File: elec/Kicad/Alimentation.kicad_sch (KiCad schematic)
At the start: 37 parts, among them J7 USB_B_Micro_MAIN, Q1 SI2323DS-T1, Q5 NTK3043NT1G, SW4 SW_ON/OFF, U9 TLV62085RLTR

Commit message: commencer le PCB vite fait
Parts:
- removed SW4: SW_ON/OFF, SINGLE_DIP_SWITCH:SW_DS04-254-2-01BK-SMT, symbol Switch:SW_SPST
- removed TP1: 3.3V, TestPoint:TestPoint_Loop_D1.80mm_Drill1.0mm_Beaded, symbol Connector:TestPoint
- removed TP3: 5V, TestPoint:TestPoint_Loop_D1.80mm_Drill1.0mm_Beaded, symbol Connector:TestPoint
- removed TP9: BAT_PERCENT, TestPoint:TestPoint_Loop_D1.80mm_Drill1.0mm_Beaded, symbol Connector:TestPoint
- added S1: SW_ON/OFF, SINGLE_DIP_SWITCH:SW_DS04-254-2-01BK-SMT, symbol DS04-254-2-01BK-SMT:DS04-254-2-01BK-SMT
- U9: footprint RLT0007A -> TLV62085RLTR:RLT0007A
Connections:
- net Vbat: now also S1.1B
- net at D7.1 (K), Q1.3 (D): now also S1.1A

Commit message: touillerie
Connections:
- net GND: now also C34.2, R31.2
- net Vbat: no longer C25.1, R4.1, R6.1, S1.1B, U9.1 (EN), U9.7 (VIN)
- net at R30.2, U9.2 (PG): no longer C34.2, R31.2
- new net Vin: C25.1, R4.1, R6.1, S1.1B, U9.1 (EN), U9.7 (VIN)
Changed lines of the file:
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@@
 	(paper "A4")
 	(junction
-		(at 27.94 57.15)
+		(at 88.9 92.71)
+		(diameter 0)
+		(color 0 0 0 0)
+	)
+	(junction
+		(at 125.73 92.71)
 		(diameter 0)
 		(color 0 0 0 0)
@@
 	)
 	(junction
+		(at 39.37 57.15)
+		(diameter 0)
+		(color 0 0 0 0)
+	)
+	(junction
 		(at 226.06 33.02)
 		(diameter 0)
@@
 	)
 	(junction
-		(at 125.73 87.63)
-		(diameter 0)
-		(color 0 0 0 0)
-	)
-	(junction
 		(at 88.9 146.05)
 		(diameter 0)
@@
 	)
 	(junction
-		(at 115.57 87.63)
-		(diameter 0)
-		(color 0 0 0 0)
-	)
-	(junction
 		(at 125.73 52.07)
 		(diameter 0)
@@
 	(wire
 		(pts
-			(xy 142.24 87.63) (xy 125.73 87.63)
+			(xy 142.24 92.71) (xy 125.73 92.71)
 		)
 		(stroke
@@
 	(wire
 		(pts
-			(xy 142.24 71.12) (xy 142.24 87.63)
+			(xy 142.24 71.12) (xy 142.24 92.71)
 		)
 		(stroke
@@
 	(wire
 		(pts
-			(xy 125.73 87.63) (xy 115.57 87.63)
-		)
-		(stroke
-			(width 0)
-			(type default)
-		)
-	)
-	(wire
-		(pts
-			(xy 27.94 57.15) (xy 44.45 57.15)
+			(xy 24.13 57.15) (xy 39.37 57.15)
 		)
 		(stroke
@@
 	(wire
 		(pts
+			(xy 88.9 92.71) (xy 125.73 92.71)
+		)
+		(stroke
+			(width 0)
+			(type default)
+		)
+	)
+	(wire
+		(pts
 			(xy 171.45 43.18) (xy 176.53 43.18)
 		)
@@
 	(wire
 		(pts
-			(xy 24.13 57.15) (xy 27.94 57.15)
-		)
-		(stroke
-			(width 0)
-			(type default)
-		)
-	)
-	(wire
-		(pts
 			(xy 77.47 146.05) (xy 88.9 146.05)
 		)
@@
 	(wire
 		(pts
-			(xy 27.94 52.07) (xy 27.94 57.15)
-		)
-		(stroke
-			(width 0)
-			(type default)
-		)
-	)
-	(wire
-		(pts
 			(xy 71.12 92.71) (xy 88.9 92.71)
 		)
@@
 	(wire
 		(pts
-			(xy 125.73 72.39) (xy 125.73 87.63)
+			(xy 125.73 72.39) (xy 125.73 92.71)
 		)
 		(stroke
@@
 		)
 	)
+	(wire
+		(pts
+			(xy 39.37 57.15) (xy 44.45 57.15)
+		)
+		(stroke
+			(width 0)
+			(type default)
+		)
+	)
 	(rectangle
 		(start 198.12 74.93)
@@
 		)
 	)
-	(global_label "Vbat"
-		(shape input)
-		(at 27.94 52.07 90)
-		(fields_autoplaced yes)
-		(effects
-			(font
-				(size 1.016 1.016)
-			)
-			(justify left)
-		)
-		(property "Intersheetrefs" "${INTERSHEET_REFS}"
-			(at 27.94 46.3922 90)
-			(effects
-				(font
-					(size 1.27 1.27)
-				)
-				(justify left)
-				(hide yes)
-			)
-		)
-	)
 	(global_label "BAT_PERCENT"
 		(shape output)
@@
 			)
 		)
-		(property "Datasheet" ""
+		(property "Datasheet" "https://www.digikey.ca/en/products/detail/onsemi/NTK3043NT1G/1484893"
 			(at 222.25 93.98 0)
 			(effects
@@
 					(unit 1)
 				)
+			)
+		)
+	)
+	(symbol
+		(lib_id "power:PWR_FLAG")
+		(at 39.37 57.15 0)
+		(unit 1)
+		(exclude_from_sim no)
+		(in_bom yes)
+		(on_board yes)
+		(dnp no)
+		(fields_autoplaced yes)
+		(property "Reference" "#FLG01"
+			(at 39.37 55.245 0)
+			(effects
+				(font
+					(size 1.27 1.27)
+				)
+				(hide yes)
+			)
+		)
+		(property "Value" "PWR_FLAG"
+			(at 39.37 52.07 0)
+			(effects
+				(font
+					(size 1.27 1.27)
+				)
+			)
+		)
+		(property "Footprint" ""
+			(at 39.37 57.15 0)
+			(effects
+				(font
+					(size 1.27 1.27)
+				)
+				(hide yes)
+			)
+		)
+		(property "Datasheet" "~"
+			(at 39.37 57.15 0)
+			(effects
+				(font
+					(size 1.27 1.27)
+				)
+				(hide yes)
+			)
+		)
+		(property "Description" "Special symbol for telling ERC where power comes from"
+			(at 39.37 57.15 0)
+			(effects
+				(font
+					(size 1.27 1.27)
+				)
+				(hide yes)
+			)
+		)
+		(pin "1"
+		)
+		(instances
+			(project "rulerSchematic"
+				(path "/a1545928-1195-40b9-b3c4-78f837012afb/47f0fc71-ff78-496f-bb04-036a9aeaa71c/6f59428e-8e72-4854-8d86-784df1ffb46d"
+					(reference "#FLG01")
+					(unit 1)
+				)

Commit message: Jpense pas boire jeudi sérieux vue que y'a pas de 5@8
routage du découplage et des CLK
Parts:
- C25, C26, C27, C28, C29, C30, C31, C32, C33, C34, C35: footprint Capacitor_SMD:C_0603_1608Metric_Pad1.08x0.95mm_HandSolder -> Capacitor_SMD:C_0402_1005Metric_Pad0.74x0.62mm_HandSolder
- R10, R11, R2, R28, R29, R30, R31, R4, R5, R6: footprint Resistor_SMD:R_0603_1608Metric_Pad0.98x0.95mm_HandSolder -> Resistor_SMD:R_0402_1005Metric_Pad0.72x0.64mm_HandSolder
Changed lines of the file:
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@@
 			)
 		)
-		(property "Footprint" "Resistor_SMD:R_0603_1608Metric_Pad0.98x0.95mm_HandSolder"
+		(property "Footprint" "Resistor_SMD:R_0402_1005Metric_Pad0.72x0.64mm_HandSolder"
 			(at 249.682 101.6 90)
 			(effects
@@
 			)
 		)
-		(property "Footprint" "Resistor_SMD:R_0603_1608Metric_Pad0.98x0.95mm_HandSolder"
+		(property "Footprint" "Resistor_SMD:R_0402_1005Metric_Pad0.72x0.64mm_HandSolder"
 			(at 234.95 94.742 90)
 			(effects
@@
 			)
 		)
-		(property "Footprint" "Capacitor_SMD:C_0603_1608Metric_Pad1.08x0.95mm_HandSolder"
+		(property "Footprint" "Capacitor_SMD:C_0402_1005Metric_Pad0.74x0.62mm_HandSolder"
 			(at 126.6952 72.39 0)
 			(effects
@@
 			)
 		)
-		(property "Footprint" "Resistor_SMD:R_0603_1608Metric_Pad0.98x0.95mm_HandSolder"
+		(property "Footprint" "Resistor_SMD:R_0402_1005Metric_Pad0.72x0.64mm_HandSolder"
 			(at 102.362 63.5 90)
 			(effects
@@
 			)
 		)
-		(property "Footprint" "Capacitor_SMD:C_0603_1608Metric_Pad1.08x0.95mm_HandSolder"
+		(property "Footprint" "Capacitor_SMD:C_0402_1005Metric_Pad0.74x0.62mm_HandSolder"
 			(at 92.4052 171.45 0)
 			(effects
@@
 			)
 		)
-		(property "Footprint" "Capacitor_SMD:C_0603_1608Metric_Pad1.08x0.95mm_HandSolder"
+		(property "Footprint" "Capacitor_SMD:C_0402_1005Metric_Pad0.74x0.62mm_HandSolder"
 			(at 113.9952 144.78 0)
 			(effects
@@
 			)
 		)
-		(property "Footprint" "Capacitor_SMD:C_0603_1608Metric_Pad1.08x0.95mm_HandSolder"
+		(property "Footprint" "Capacitor_SMD:C_0402_1005Metric_Pad0.74x0.62mm_HandSolder"
 			(at 65.7352 144.78 0)
 			(effects
@@
 			)
 		)
-		(property "Footprint" "Resistor_SMD:R_0603_1608Metric_Pad0.98x0.95mm_HandSolder"
+		(property "Footprint" "Resistor_SMD:R_0402_1005Metric_Pad0.72x0.64mm_HandSolder"
 			(at 221.488 109.22 90)
 			(effects
@@
 			)
 		)
-		(property "Footprint" "Capacitor_SMD:C_0603_1608Metric_Pad1.08x0.95mm_HandSolder"
+		(property "Footprint" "Capacitor_SMD:C_0402_1005Metric_Pad0.74x0.62mm_HandSolder"
 			(at 78.4352 144.78 0)
 			(effects
@@
 			)
 		)
-		(property "Footprint" "Resistor_SMD:R_0603_1608Metric_Pad0.98x0.95mm_HandSolder"
+		(property "Footprint" "Resistor_SMD:R_0402_1005Metric_Pad0.72x0.64mm_HandSolder"
 			(at 221.488 82.55 90)
 			(effects
@@
 			)
 		)
-		(property "Footprint" "Capacitor_SMD:C_0603_1608Metric_Pad1.08x0.95mm_HandSolder"
+		(property "Footprint" "Capacitor_SMD:C_0402_1005Metric_Pad0.74x0.62mm_HandSolder"
 			(at 196.5452 45.72 0)
 			(effects
@@
 			)
 		)
-		(property "Footprint" "Capacitor_SMD:C_0603_1608Metric_Pad1.08x0.95mm_HandSolder"
+		(property "Footprint" "Capacitor_SMD:C_0402_1005Metric_Pad0.74x0.62mm_HandSolder"
 			(at 103.8352 171.45 0)
 			(effects
@@
 			)
 		)
-		(property "Footprint" "Resistor_SMD:R_0603_1608Metric_Pad0.98x0.95mm_HandSolder"
+		(property "Footprint" "Resistor_SMD:R_0402_1005Metric_Pad0.72x0.64mm_HandSolder"
 			(at 113.792 68.58 90)
 			(effects
@@
 			)
 		)
-		(property "Footprint" "Resistor_SMD:R_0603_1608Metric_Pad0.98x0.95mm_HandSolder"
+		(property "Footprint" "Resistor_SMD:R_0402_1005Metric_Pad0.72x0.64mm_HandSolder"
 			(at 208.788 41.91 90)
 			(effects
@@
 			)
 		)
-		(property "Footprint" "Capacitor_SMD:C_0603_1608Metric_Pad1.08x0.95mm_HandSolder"
+		(property "Footprint" "Capacitor_SMD:C_0402_1005Metric_Pad0.74x0.62mm_HandSolder"
 			(at 101.2952 144.78 0)
 			(effects
@@
 			)
 		)
-		(property "Footprint" "Resistor_SMD:R_0603_1608Metric_Pad0.98x0.95mm_HandSolder"
+		(property "Footprint" "Resistor_SMD:R_0402_1005Metric_Pad0.72x0.64mm_HandSolder"
 			(at 227.838 43.18 90)
 			(effects
@@
 			)
 		)
-		(property "Footprint" "Resistor_SMD:R_0603_1608Metric_Pad0.98x0.95mm_HandSolder"
+		(property "Footprint" "Resistor_SMD:R_0402_1005Metric_Pad0.72x0.64mm_HandSolder"
 			(at 140.462 67.31 90)
 			(effects
@@
 			)
 		)
-		(property "Footprint" "Resistor_SMD:R_0603_1608Metric_Pad0.98x0.95mm_HandSolder"
+		(property "Footprint" "Resistor_SMD:R_0402_1005Metric_Pad0.72x0.64mm_HandSolder"
 			(at 102.362 78.74 90)
 			(effects
@@
 			)
 		)
-		(property "Footprint" "Capacitor_SMD:C_0603_1608Metric_Pad1.08x0.95mm_HandSolder"
+		(property "Footprint" "Capacitor_SMD:C_0402_1005Metric_Pad0.74x0.62mm_HandSolder"
 			(at 45.4152 71.12 0)
 			(effects
@@
 			)
 		)
-		(property "Footprint" "Capacitor_SMD:C_0603_1608Metric_Pad1.08x0.95mm_HandSolder"
+		(property "Footprint" "Capacitor_SMD:C_0402_1005Metric_Pad0.74x0.62mm_HandSolder"
 			(at 125.4252 144.78 0)
 			(effects
@@
 			)
 		)
-		(property "Footprint" "Capacitor_SMD:C_0603_1608Metric_Pad1.08x0.95mm_HandSolder"
+		(property "Footprint" "Capacitor_SMD:C_0402_1005Metric_Pad0.74x0.62mm_HandSolder"
 			(at 89.8652 144.78 0)
 			(effects

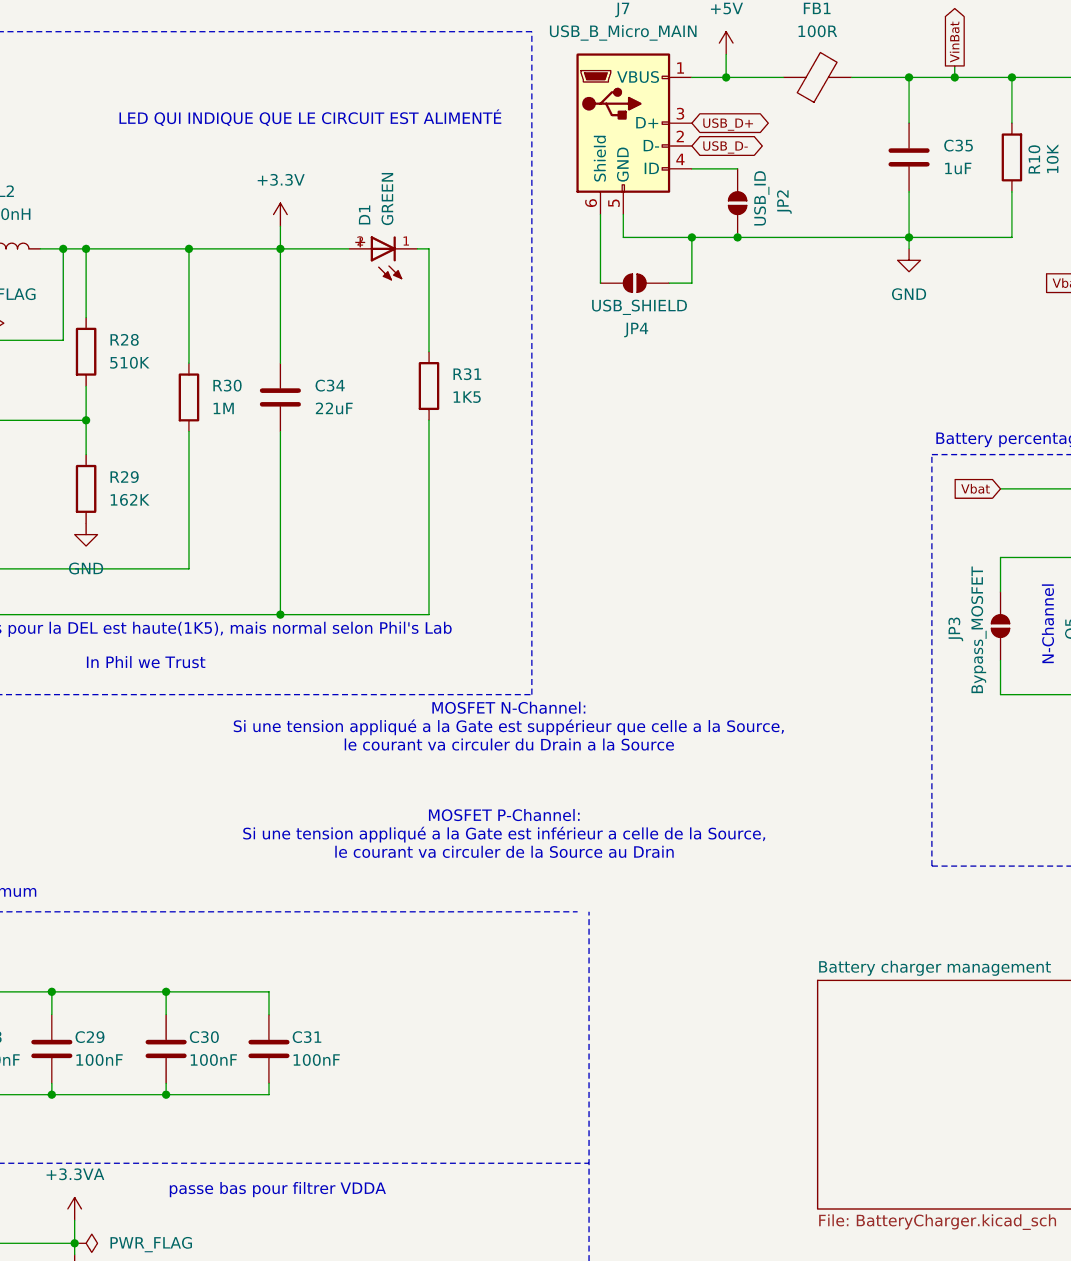
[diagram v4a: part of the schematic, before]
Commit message: modification du magnéto
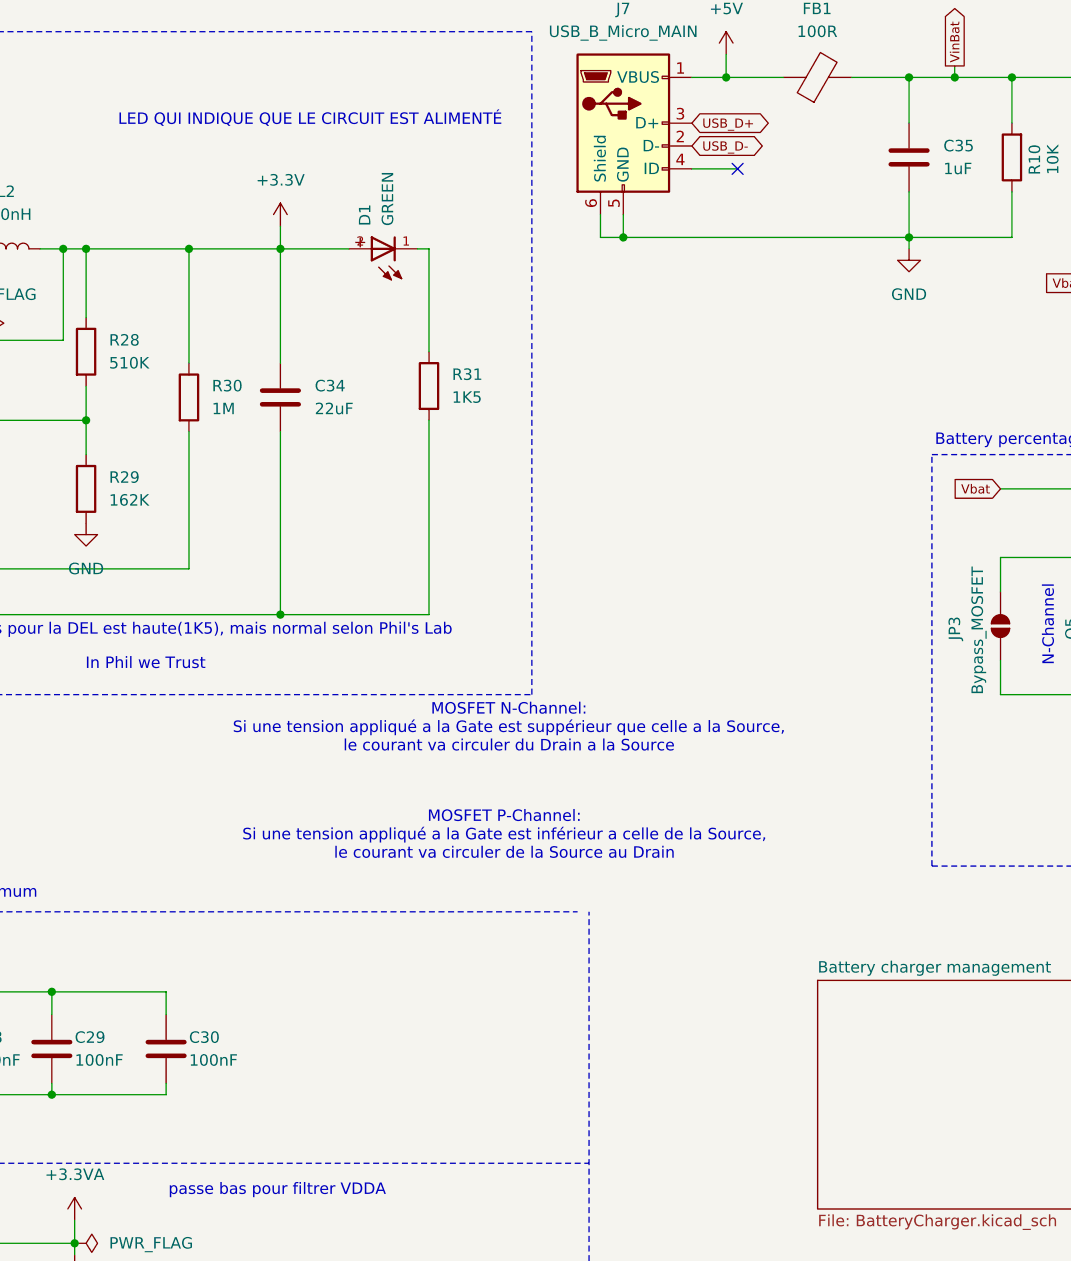
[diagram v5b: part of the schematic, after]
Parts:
- removed C31: 100nF, Capacitor_SMD:C_0402_1005Metric_Pad0.74x0.62mm_HandSolder, symbol Device:C
- removed JP2: USB_ID, Jumper:SolderJumper-2_P1.3mm_Open_TrianglePad1.0x1.5mm, symbol Jumper:SolderJumper_2_Open
- removed JP4: USB_SHIELD, Jumper:SolderJumper-2_P1.3mm_Open_TrianglePad1.0x1.5mm, symbol Jumper:SolderJumper_2_Open
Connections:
- net GND: now also J7.6 (Shield)
- no-connect marks 0 -> 1

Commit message: abdel aziz clutch l'app5
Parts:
- removed JP3: Bypass_MOSFET, Jumper:SolderJumper-2_P1.3mm_Open_TrianglePad1.0x1.5mm, symbol Jumper:SolderJumper_2_Open
- added R18: Bypass_MOSFET (0 ohm), Resistor_SMD:R_0201_0603Metric, symbol Device:R
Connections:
- net BAT_PERCENT: now also R18.1
- net at Q5.3, R2.1: now also R18.2
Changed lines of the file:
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@@
-	)
-	(symbol
-		(lib_id "Jumper:SolderJumper_2_Open")
-		(at 205.74 93.98 270)
-		(unit 1)
-		(exclude_from_sim yes)
-		(in_bom no)
-		(on_board yes)
-		(dnp no)
-		(property "Reference" "JP3"
-			(at 200.66 94.234 0)
-			(effects
-				(font
-					(size 1.27 1.27)
-				)
-			)
-		)
-		(property "Value" "Bypass_MOSFET"
-			(at 203.2 94.488 0)
-			(effects
-				(font
-					(size 1.27 1.27)
-				)
-			)
-		)
-		(property "Footprint" "Jumper:SolderJumper-2_P1.3mm_Open_TrianglePad1.0x1.5mm"
-			(at 205.74 93.98 0)
-			(effects
-				(font
-					(size 1.27 1.27)
-				)
-				(hide yes)
-			)
-		)
-		(property "Datasheet" "~"
-			(at 205.74 93.98 0)
-			(effects
-				(font
-					(size 1.27 1.27)
-				)
-				(hide yes)
-			)
-		)
-		(property "Description" "Solder Jumper, 2-pole, open"
-			(at 205.74 93.98 0)
-			(effects
-				(font
-					(size 1.27 1.27)
-				)
-				(hide yes)
-			)
-		)
-		(pin "2"
-		)
-		(pin "1"
-		)
-		(instances
-			(project "rulerSchematic"
-				(path "/a1545928-1195-40b9-b3c4-78f837012afb/47f0fc71-ff78-496f-bb04-036a9aeaa71c/6f59428e-8e72-4854-8d86-784df1ffb46d"
-					(reference "JP3")
-					(unit 1)
-				)
-			)
-		)
 	)
 	(symbol
@@
 					(unit 1)
 				)
+			)
+		)
+	)
+	(symbol
+		(lib_id "Device:R")
+		(at 205.74 93.98 180)
+		(unit 1)
+		(exclude_from_sim no)
+		(in_bom yes)
+		(on_board yes)
+		(dnp no)
+		(property "Reference" "R18"
+			(at 208.28 94.234 90)
+			(effects
+				(font
+					(size 1.27 1.27)
+				)
+			)
+		)
+		(property "Value" "Bypass_MOSFET (0 ohm)"
+			(at 202.946 93.98 90)
+			(effects
+				(font
+					(size 1.27 1.27)
+				)
+			)
+		)
+		(property "Footprint" "Resistor_SMD:R_0201_0603Metric"
+			(at 207.518 93.98 90)
+			(effects
+				(font
+					(size 1.27 1.27)
+				)
+				(hide yes)
+			)
+		)
+		(property "Datasheet" "~"
+			(at 205.74 93.98 0)
+			(effects
+				(font
+					(size 1.27 1.27)
+				)
+				(hide yes)
+			)
+		)
+		(property "Description" ""
+			(at 205.74 93.98 0)
+			(effects
+				(font
+					(size 1.27 1.27)
+				)
+				(hide yes)
+			)
+		)
+		(pin "1"
+		)
+		(pin "2"
+		)
+		(instances
+			(project "rulerSchematic"
+				(path "/a1545928-1195-40b9-b3c4-78f837012afb/47f0fc71-ff78-496f-bb04-036a9aeaa71c/6f59428e-8e72-4854-8d86-784df1ffb46d"
+					(reference "R18")
+					(unit 1)
+				)

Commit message: j'essaye de fix la hauteur des designator pis si sa scrap cv être ça
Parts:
- L1: footprint LQP03TN27NJ02D:INDC0603X33N -> LQG15HN27NJ02D:INDC1005X55N
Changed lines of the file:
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@@
 			)
 		)
-		(property "Footprint" "LQP03TN27NJ02D:INDC0603X33N"
+		(property "Footprint" "LQG15HN27NJ02D:INDC1005X55N"
 			(at 80.01 162.56 0)
 			(effects
@@
 			)
 		)
-		(property "Datasheet" "https://www.digikey.ca/en/products/detail/murata-electronics/LQP03TN27NJ02D/2357643"
+		(property "Datasheet" "https://www.digikey.ca/en/products/detail/murata-electronics/LQG15HN27NJ02D/584299?"
 			(at 80.01 162.56 0)
 			(effects

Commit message: généré la schematic
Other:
- note added: "Vin = 5V (si USB branché) Vbat = entre 4.2V et 3.5V"
- note removed: "In Phil we Trust"
- note removed: "La valeur de la res pour la DEL est haute(1K5), mais normal selon Phil's Lab"
- note removed: "METTRE DES SWITCH POUR ÉTEINDRE LE CIRCUIT + avoir une scroll wheel vrm bs pour les menu (et la magouille ultime)"
- note removed: "Vin = 5V Vbat = entre 4.2V et 3.5V"
- company: (none) -> University of Sherbrooke
- title: (none) -> Touillomètre - Power Management
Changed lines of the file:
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@@
 	(generator_version "8.0")
 	(paper "A4")
+	(title_block
+		(title "Touillomètre - Power Management")
+		(date "2024-12-26")
+		(rev "C3I")
+		(company "University of Sherbrooke")
+	)
 	(junction
 		(at 88.9 92.71)
@@
 	(rectangle
 		(start 198.12 74.93)
-		(end 275.59 120.65)
+		(end 275.59 123.19)
 		(stroke
 			(width 0)
@@
 		)
 	)
-	(text "Vin = 5V\nVbat = entre 4.2V et 3.5V"
+	(text "Vin = 5V (si USB branché)\nVbat = entre 4.2V et 3.5V"
 		(exclude_from_sim no)
 		(at 30.48 38.862 0)
@@
 		)
 	)
-	(text "In Phil we Trust"
-		(exclude_from_sim no)
-		(at 110.744 98.298 0)
-		(effects
-			(font
-				(size 1.27 1.27)
-			)
-		)
-	)
-	(text "METTRE DES SWITCH POUR ÉTEINDRE LE CIRCUIT + avoir une scroll wheel vrm bs pour les menu (et la magouille ultime)"
-		(exclude_from_sim no)
-		(at 74.676 17.78 0)
-		(effects
-			(font
-				(size 1.27 1.27)
-			)
-		)
-	)
 	(text "Battery percentage charger\n"
 		(exclude_from_sim no)
@@
 	(text "LED QUI INDIQUE QUE LE CIRCUIT EST ALIMENTÉ"
 		(exclude_from_sim no)
-		(at 129.032 37.846 0)
-		(effects
-			(font
-				(size 1.27 1.27)
-			)
-		)
-	)
-	(text "La valeur de la res pour la DEL est haute(1K5), mais normal selon Phil's Lab "
-		(exclude_from_sim no)
-		(at 111.76 94.488 0)
+		(at 128.778 39.624 0)
 		(effects
 			(font
@@
 	(text "MOSFET N-Channel:\nSi une tension appliqué a la Gate est suppérieur que celle a la Source,\nle courant va circuler du Drain a la Source"
 		(exclude_from_sim no)
-		(at 151.13 105.41 0)
+		(at 151.638 108.966 0)
 		(effects
 			(font
